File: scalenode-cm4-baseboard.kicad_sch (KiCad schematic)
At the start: 2 parts

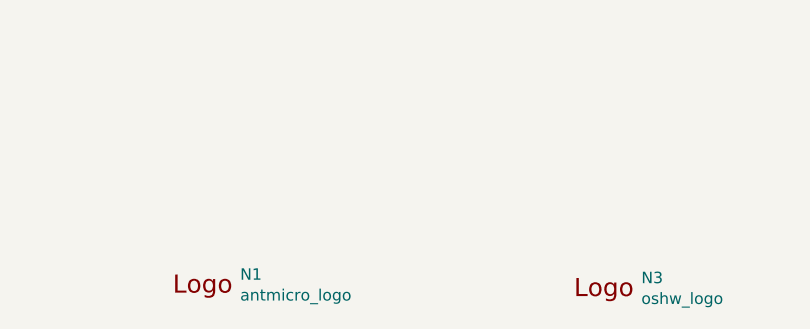
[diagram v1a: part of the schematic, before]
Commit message: Update N1, N3 symbol and footprint
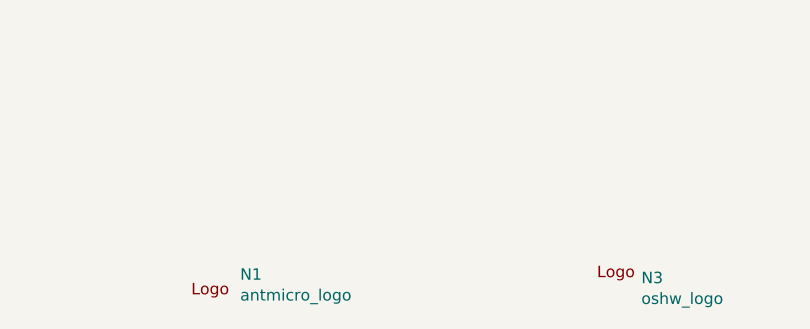
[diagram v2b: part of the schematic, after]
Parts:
- N1: footprint scalenode-cm4-baseboard-footprints:antmicro-logo_scaled_15mm -> antmicro-footprints:antmicro-logo; symbol scalenode-cm4-baseboard:antmicro_logo -> antmicroMechanicalParts:antmicro_logo; Author (none) -> Antmicro; License (none) -> Apache-2.0; Manufacturer (none) -> None
- N3: footprint scalenode-cm4-baseboard-footprints:oshw-logo -> antmicro-footprints:oshw-logo; symbol scalenode-cm4-baseboard:oshw_logo -> antmicroMechanicalParts:oshw_logo; Author (none) -> Antmicro; License (none) -> Apache-2.0; Manufacturer (none) -> None
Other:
- moved on the sheet: N1, N3
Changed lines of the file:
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@@
     )
   )
-  (symbol (lib_id "scalenode-cm4-baseboard:antmicro_logo") (at 98.171 273.685 0) (unit 1)
+  (symbol (lib_id "antmicroMechanicalParts:antmicro_logo") (at 98.171 273.685 0) (unit 1)
     (in_bom yes) (on_board yes)
     (property "Reference" "N1" (id 0) (at 103.6066 271.3228 0)
@@
       (effects (font (size 1.27 1.27)) (justify left))
     )
-    (property "Footprint" "scalenode-cm4-baseboard-footprints:antmicro-logo_scaled_15mm" (id 2) (at 95.631 267.335 0)
-      (effects (font (size 1.27 1.27)) hide)
-    )
-    (property "Datasheet" "" (id 3) (at 98.171 264.795 0)
-      (effects (font (size 1.27 1.27)) hide)
-    )
-  )
-  (symbol (lib_id "scalenode-cm4-baseboard:oshw_logo") (at 143.256 271.78 0) (unit 1)
+    (property "Footprint" "antmicro-footprints:antmicro-logo" (id 2) (at 113.411 283.845 0)
+      (effects (font (size 1.27 1.27) (thickness 0.15)) (justify left bottom) hide)
+    )
+    (property "Datasheet" "" (id 3) (at 113.411 286.385 0)
+      (effects (font (size 1.27 1.27) (thickness 0.15)) (justify left bottom) hide)
+    )
+    (property "Author" "Antmicro" (id 4) (at 113.411 288.925 0)
+      (effects (font (size 1.27 1.27) (thickness 0.15)) (justify left bottom) hide)
+    )
+    (property "License" "Apache-2.0" (id 5) (at 113.411 291.465 0)
+      (effects (font (size 1.27 1.27) (thickness 0.15)) (justify left bottom) hide)
+    )
+    (property "Manufacturer" "None" (id 6) (at 113.411 294.005 0)
+      (effects (font (size 1.27 1.27) (thickness 0.15)) (justify left bottom) hide)
+    )
+  )
+  (symbol (lib_id "antmicroMechanicalParts:oshw_logo") (at 143.256 271.78 0) (unit 1)
     (in_bom yes) (on_board yes)
     (property "Reference" "N3" (id 0) (at 148.1836 271.7038 0)
@@
       (effects (font (size 1.27 1.27)) (justify left))
     )
-    (property "Footprint" "scalenode-cm4-baseboard-footprints:oshw-logo" (id 2) (at 143.764 277.876 0)
-      (effects (font (size 1.27 1.27)) hide)
-    )
-    (property "Datasheet" "" (id 3) (at 143.256 271.78 0)
-      (effects (font (size 1.27 1.27)) hide)
+    (property "Footprint" "antmicro-footprints:oshw-logo" (id 2) (at 158.496 281.94 0)
+      (effects (font (size 1.27 1.27) (thickness 0.15)) (justify left bottom) hide)
+    )
+    (property "Datasheet" "" (id 3) (at 158.496 284.48 0)
+      (effects (font (size 1.27 1.27) (thickness 0.15)) (justify left bottom) hide)
+    )
+    (property "Author" "Antmicro" (id 4) (at 158.496 287.02 0)
+      (effects (font (size 1.27 1.27) (thickness 0.15)) (justify left bottom) hide)
+    )
+    (property "License" "Apache-2.0" (id 5) (at 158.496 289.56 0)
+      (effects (font (size 1.27 1.27) (thickness 0.15)) (justify left bottom) hide)
+    )
+    (property "Manufacturer" "None" (id 6) (at 158.496 292.1 0)
+      (effects (font (size 1.27 1.27) (thickness 0.15)) (justify left bottom) hide)
     )
   )
@@
     )
     (path "/00000000-0000-0000-0000-0000602d4d74"
-      (reference "N1") (unit 1) (value "antmicro_logo") (footprint "scalenode-cm4-baseboard-footprints:antmicro-logo_scaled_15mm")
+      (reference "N1") (unit 1) (value "antmicro_logo") (footprint "antmicro-footprints:antmicro-logo")
     )
     (path "/00000000-0000-0000-0000-0000603350d4"
-      (reference "N3") (unit 1) (value "oshw_logo") (footprint "scalenode-cm4-baseboard-footprints:oshw-logo")
+      (reference "N3") (unit 1) (value "oshw_logo") (footprint "antmicro-footprints:oshw-logo")
     )
     (path "/00000000-0000-0000-0000-00005fea17d8/fc872f03-bc7c-4dd0-9228-6ff7b64fca40"
